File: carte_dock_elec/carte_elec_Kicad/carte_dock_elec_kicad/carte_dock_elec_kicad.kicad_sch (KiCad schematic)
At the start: 0 parts

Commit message: Modif_carte_elec
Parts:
- added D1: D, Diode_SMD:D_0201_0603Metric, symbol Device:D
- added J1, J2, J3: Conn_01x02_Pin, Connector:JWT_A3963_1x02_P3.96mm_Vertical, symbol Connector:Conn_01x02_Pin
- added J4, J5, J6: Conn_01x04_Pin, Connector:FanPinHeader_1x04_P2.54mm_Vertical, symbol Connector:Conn_01x04_Pin
- added J7, J8, J9: 1758018, CONN_1758018, symbol Library_carte_elec:1758018
- added Q1: IRLB8748PBF, TO254P483X1016X1994-3P, symbol Library_carte_elec:IRLB8748PBF
- added R1: 10k, symbol Device:R
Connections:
- new net: D1.2 (A), J7.2, J8.2, Q1.2 (D)
- new net: D1.1 (K), J1.1 (Pin_1), J2.1 (Pin_1), J7.1, J8.1
- new net 3.3V: J5.1 (Pin_1), J6.1 (Pin_1)
- new net 5V: J4.2 (Pin_2), J9.2, R1.1
- new net GND: J1.2 (Pin_2), J2.2 (Pin_2), J3.1 (Pin_1), J4.1 (Pin_1), J5.4 (Pin_4), J6.4 (Pin_4), J9.1, Q1.3 (S)
- new net PIN11: J4.4 (Pin_4)
- new net PIN13: J3.2 (Pin_2), R1.2
- new net PIN15: Q1.1 (G)
- new net SCL: J5.3 (Pin_3), J6.3 (Pin_3)
- new net SDA: J5.2 (Pin_2), J6.2 (Pin_2)
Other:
- note added: "Changer les connecteurs et importer les bonnes empreintes/ symboles"

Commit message: Modif_schema_creationPCB
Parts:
- removed J1, J2, J3: Conn_01x02_Pin, Connector:JWT_A3963_1x02_P3.96mm_Vertical, symbol Connector:Conn_01x02_Pin
- removed J4, J5, J6: Conn_01x04_Pin, Connector:FanPinHeader_1x04_P2.54mm_Vertical, symbol Connector:Conn_01x04_Pin
- added J1, J6: 1758018, Librarie_empreinte:CONN_1758018, symbol Library_carte_elec:1758018
- added J10: Conn_02x20_Odd_Even, Connector_PinSocket_2.54mm:PinSocket_2x20_P2.54mm_Vertical, symbol Connector_Generic:Conn_02x20_Odd_Even
- added J2: 22053021, Librarie_empreinte:CONN_A-7478-02A_MOL, symbol Library_carte_elec:22053021
- added J3, J4, J5: 22272041, Librarie_empreinte:CONN_AE-6410-04A_MOL, symbol Library_carte_elec:22272041
- J7, J8, J9: footprint CONN_1758018 -> Librarie_empreinte:CONN_1758018
- R1: footprint (none) -> Resistor_SMD:R_0201_0603Metric
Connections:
- net 3.3V: now also J10.1 (Pin_1), J3.4, J5.4
- net 5V: now also J10.2 (Pin_2), J10.4 (Pin_4), J4.3
- net GND: now also J1.1, J2.2, J3.1, J4.4, J5.1, J6.1
- net PIN11: now also J10.11 (Pin_11), J4.1
- net PIN13: now also J10.13 (Pin_13), J2.1
- net PIN15: now also J10.15 (Pin_15)
- net SCL: now also J10.5 (Pin_5), J3.2, J5.2
- net SDA: now also J10.3 (Pin_3), J3.3, J5.3
- net at D1.1 (K), J7.1, J8.1: now also J1.2, J6.2
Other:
- note added: "Alimentation 20V"
- note added: "Alimentation carte"
- note added: "Carte de chargement TIBQ25887EVM"
- note added: "Ecran OLED TF051"
- note added: "Electroaimants (x2) Mecalectro C201000651"
- note added: "Pogo pin (interrepteur de détection du ballon)"
- note added: "RPI4"
- note added: "Ventilateur"
- note removed: "Changer les connecteurs et importer les bonnes empreintes/ symboles"

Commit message: carte_dock
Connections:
- net 3.3V: now also J10.2 (Pin_2); no longer J10.1 (Pin_1)
- net 5V: now also J10.1 (Pin_1), J10.3 (Pin_3); no longer J10.2 (Pin_2), J10.4 (Pin_4)
- net PIN11: now also J10.12 (Pin_12); no longer J10.11 (Pin_11)
- net PIN13: now also J10.14 (Pin_14); no longer J10.13 (Pin_13)
- net PIN15: now also J10.16 (Pin_16); no longer J10.15 (Pin_15)
- net SCL: now also J10.6 (Pin_6); no longer J10.5 (Pin_5)
- net SDA: now also J10.4 (Pin_4); no longer J10.3 (Pin_3)
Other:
- moved on the sheet: J10

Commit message: MAJ DOCK ELEC
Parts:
- D1: footprint Diode_SMD:D_0201_0603Metric -> Diode_SMD:D_1206_3216Metric
- R1: footprint Resistor_SMD:R_0201_0603Metric -> Resistor_SMD:R_1206_3216Metric
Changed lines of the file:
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@@
 			)
 		)
-		(property "Footprint" "Diode_SMD:D_0201_0603Metric"
+		(property "Footprint" "Diode_SMD:D_1206_3216Metric"
 			(at 97.79 123.19 0)
 			(hide yes)
@@
 			)
 		)
-		(property "Footprint" "Resistor_SMD:R_0201_0603Metric"
+		(property "Footprint" "Resistor_SMD:R_1206_3216Metric"
 			(at 80.01 80.518 90)
 			(hide yes)

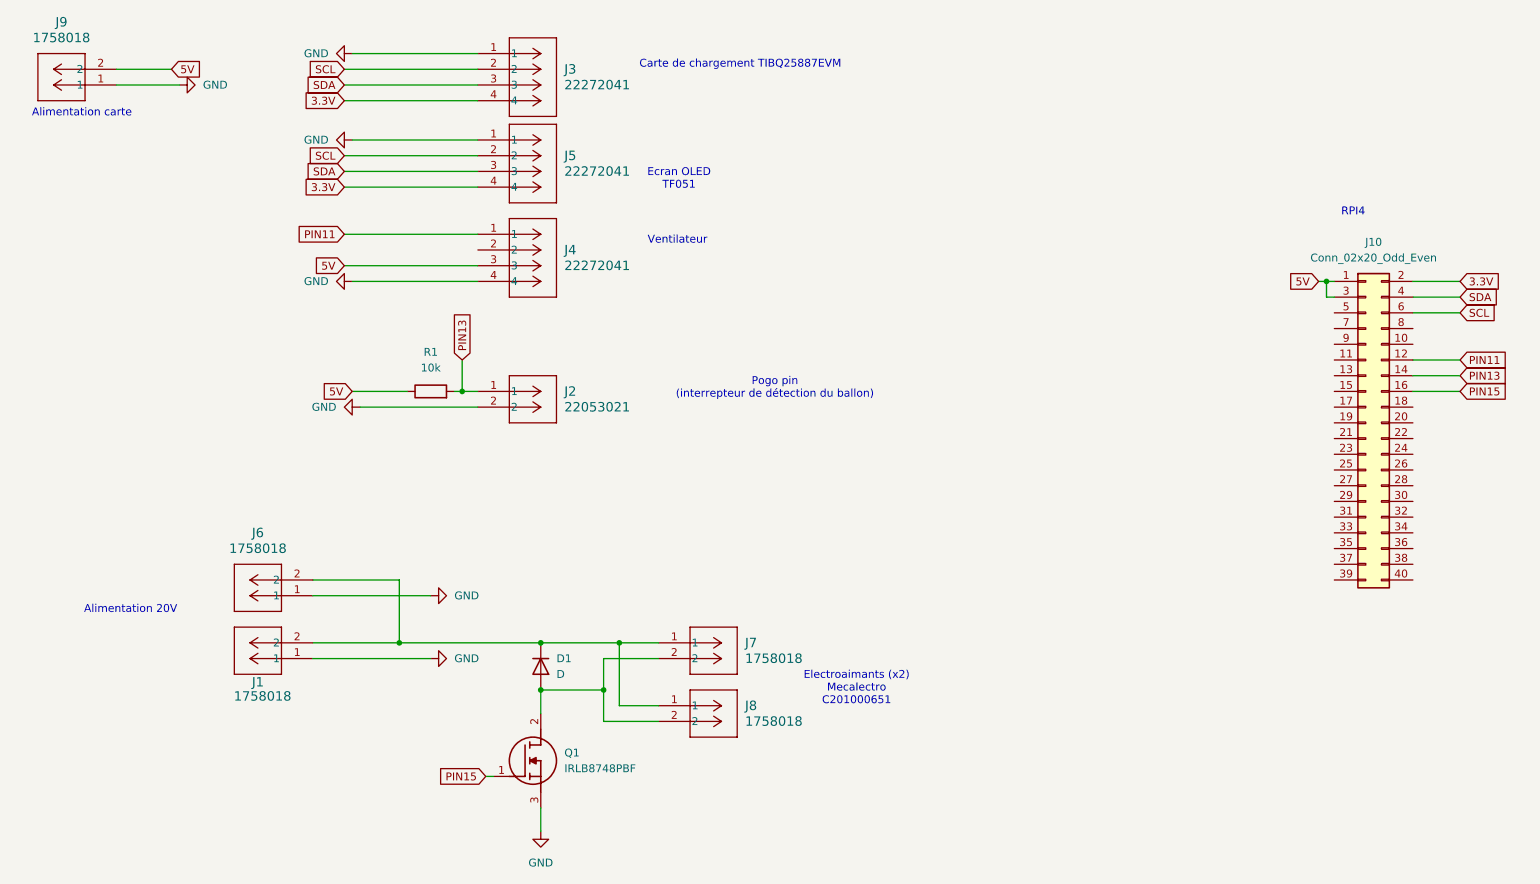
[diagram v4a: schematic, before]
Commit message: Modif_carte_dock
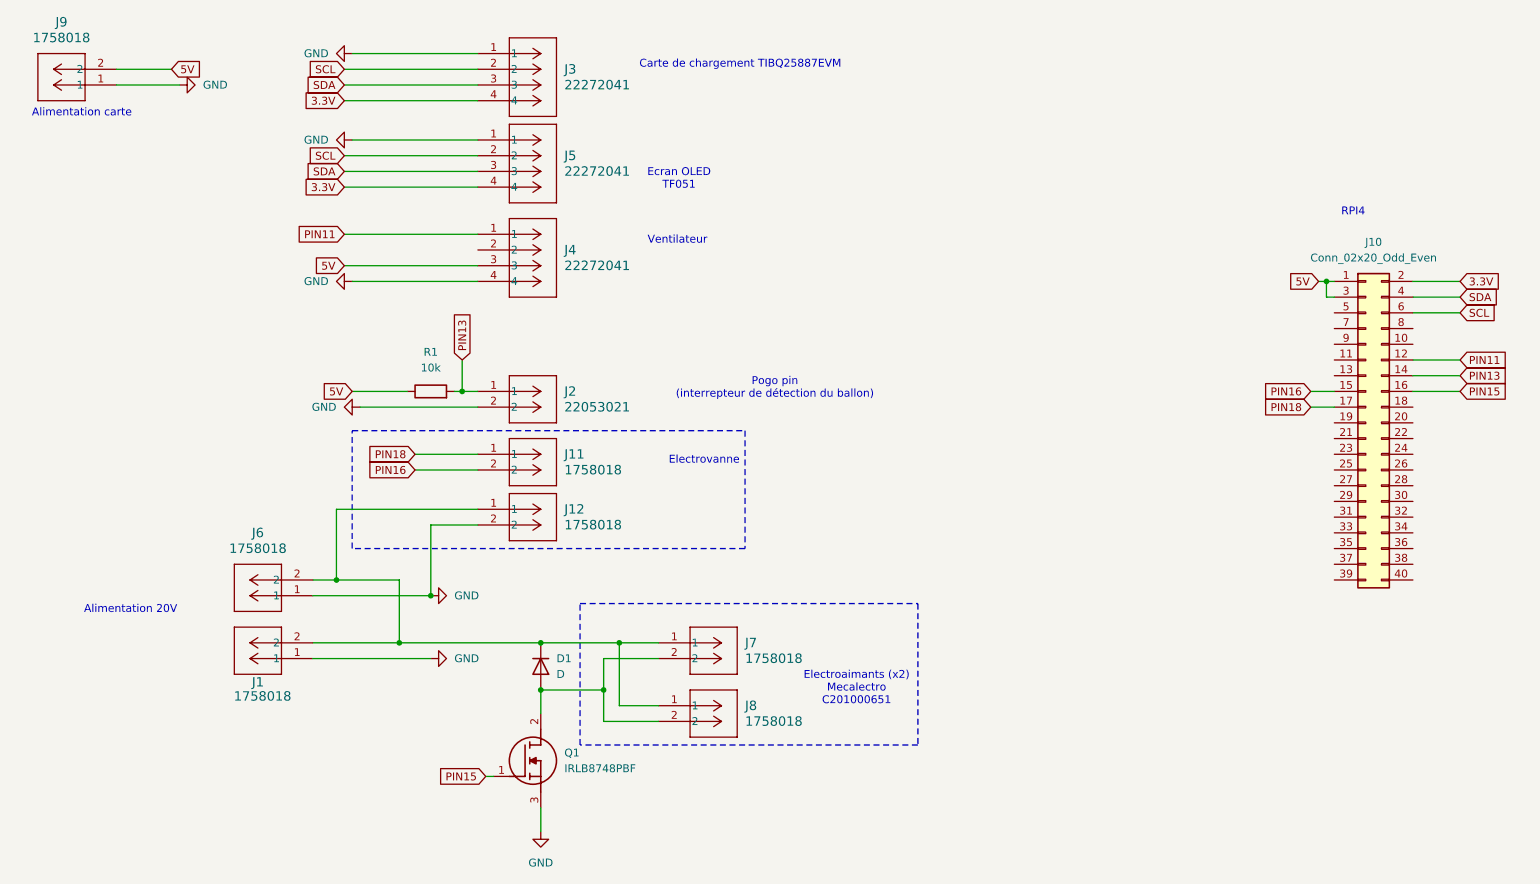
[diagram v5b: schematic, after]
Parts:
- added J11, J12: 1758018, Librarie_empreinte:CONN_1758018, symbol Library_carte_elec:1758018
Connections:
- net GND: now also J12.2
- net PIN16: now reaches J10.15 (Pin_15)
- net PIN16: now also J11.2
- net PIN18: now reaches J10.17 (Pin_17)
- net PIN18: now also J11.1
- net at D1.1 (K), J1.2, J6.2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: now also J12.1
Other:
- note added: "Electrovanne"

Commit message: rapport
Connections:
- net PIN16: now also J11.1; no longer J11.2
- net PIN29: now reaches J10.30 (Pin_30)
- net PIN29: now also J11.2
- net PIN18: no longer names the net of J10.17 (Pin_17)
- net PIN18: no longer J11.1
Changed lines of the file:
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@@
+		)
+	)
+	(wire
+		(pts
+			(xy 238.76 96.52) (xy 247.65 96.52)
+		)
+		(stroke
+			(width 0)
+			(type default)
 		)
 	)
@@
 		)
 	)
-	(global_label "PIN18"
+	(global_label "PIN16"
 		(shape input)
 		(at 77.47 88.9 180)
@@
 		)
 	)
-	(global_label "PIN18"
-		(shape input)
-		(at 222.25 81.28 180)
-		(fields_autoplaced yes)
-		(effects
-			(font
-				(size 1.27 1.27)
-			)
-			(justify right)
-		)
-		(property "Intersheetrefs" "${INTERSHEET_REFS}"
-			(at 213.6405 81.28 0)
-			(hide yes)
-			(show_name no)
-			(do_not_autoplace no)
-			(effects
-				(font
-					(size 1.27 1.27)
-				)
-				(justify right)
-			)
-		)
-	)
 	(global_label "PIN13"
 		(shape input)
@@
 		)
 	)
-	(global_label "PIN16"
+	(global_label "PIN29"
 		(shape input)
 		(at 77.47 91.44 180)
@@
 			)
 		)
+	)
+	(global_label "PIN29"
+		(shape input)
+		(at 247.65 96.52 0)
+		(fields_autoplaced yes)
+		(effects
+			(font
+				(size 1.27 1.27)
+			)
+			(justify left)
+		)
+		(property "Intersheetrefs" "${INTERSHEET_REFS}"
+			(at 256.2595 96.52 0)
+			(hide yes)
+			(show_name no)
+			(do_not_autoplace no)
+			(effects
+				(font
+					(size 1.27 1.27)
+				)
+				(justify left)
+			)
+		)

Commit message: modif_carte_dick
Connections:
- net GND: now also J10.5 (Pin_5)
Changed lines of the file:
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@@
+	(wire
+		(pts
+			(xy 223.52 66.04) (xy 226.06 66.04)
+		)
+		(stroke
+			(width 0)
+			(type default)
+		)
+	)
 	(wire
 		(pts
@@
 		)
 	)
+	(global_label "GND"
+		(shape input)
+		(at 223.52 66.04 180)
+		(fields_autoplaced yes)
+		(effects
+			(font
+				(size 1.27 1.27)
+			)
+			(justify right)
+		)
+		(property "Intersheetrefs" "${INTERSHEET_REFS}"
+			(at 216.6643 66.04 0)
+			(hide yes)
+			(show_name no)
+			(do_not_autoplace no)
+			(effects
+				(font
+					(size 1.27 1.27)
+				)
+				(justify right)
+			)
+		)
+	)
